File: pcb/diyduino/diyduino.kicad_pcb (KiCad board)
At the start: 2 copper layers, 22 parts, among them U1 ATMEGA328-PU, U2 L7805, Y1 16MHz

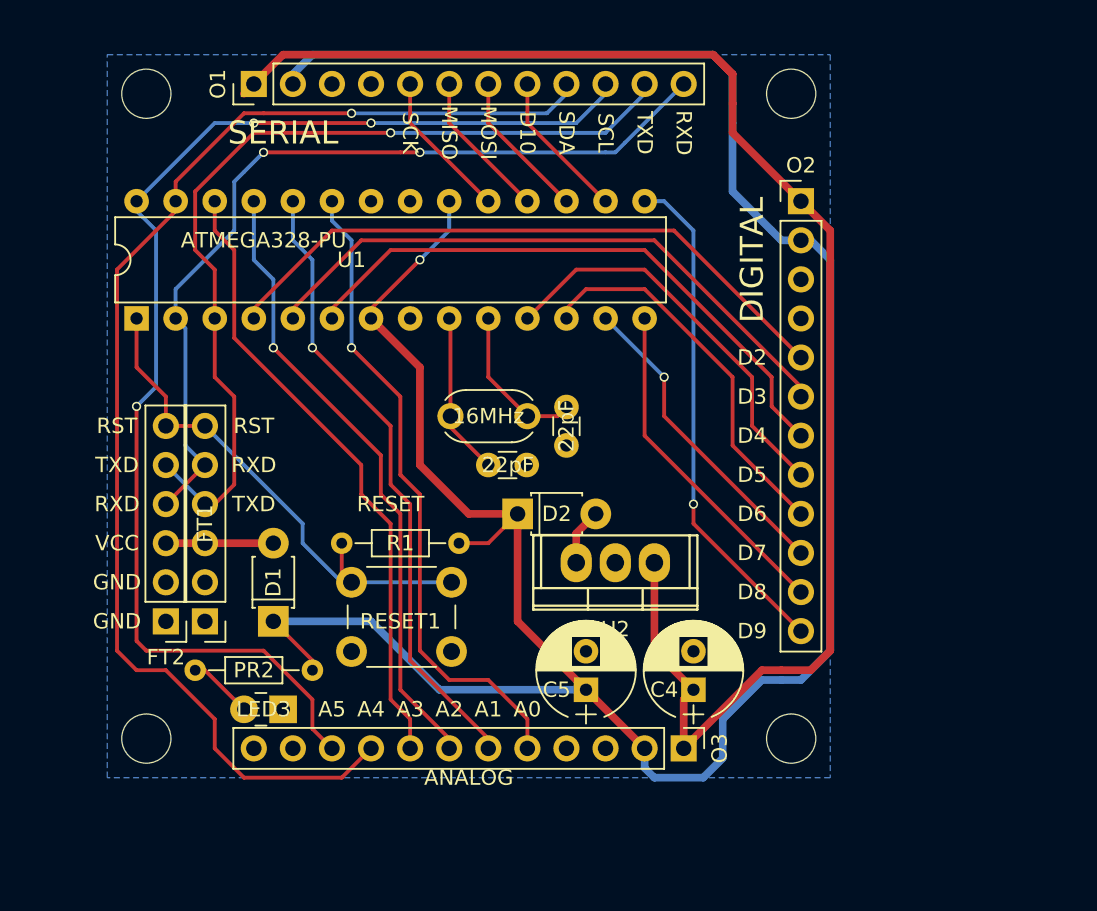
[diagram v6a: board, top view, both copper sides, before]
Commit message: Added a Rotary Encoder module. Tidied up a couple of modules before printing them.
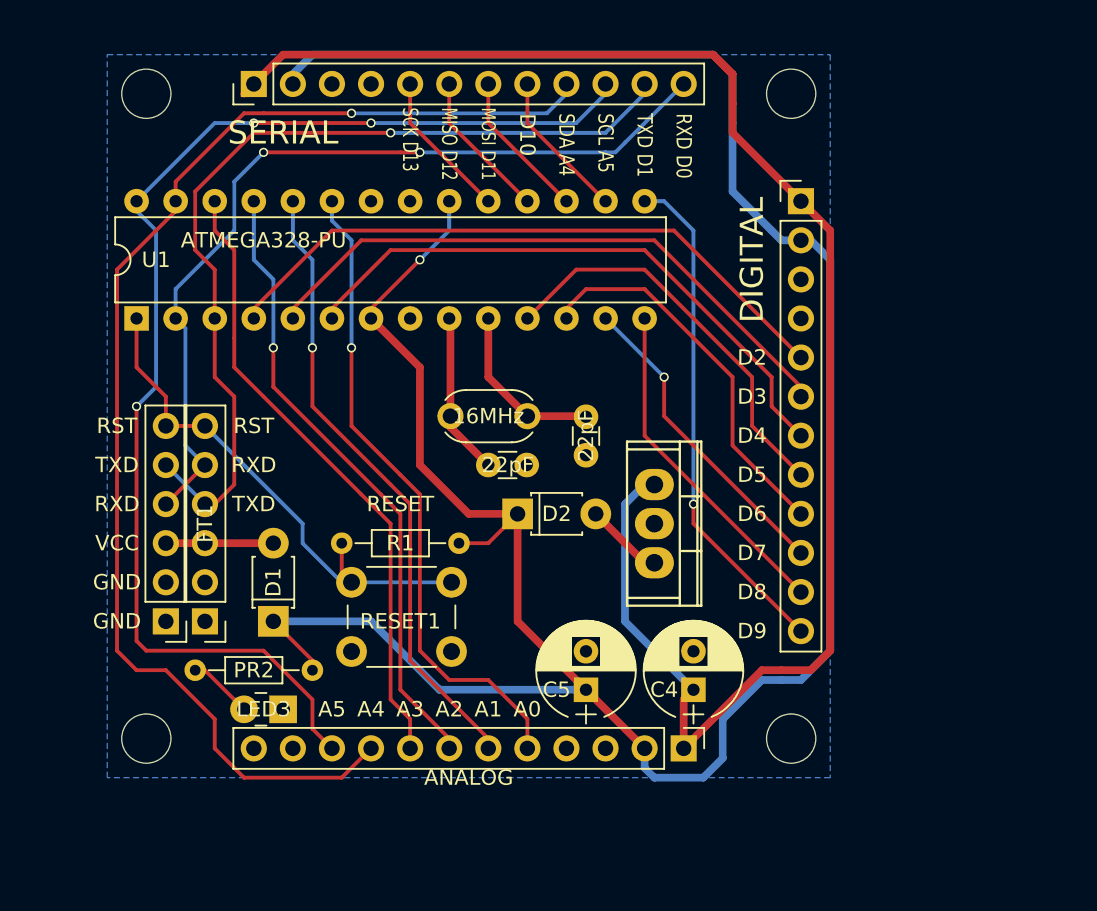
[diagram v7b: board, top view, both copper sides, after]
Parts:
- moved U2 3.59 mm to (145.4, 62.9), turned to 270 degrees
- moved C3 1.42 mm to (141.0, 58.4)
- gave numbers to parts that had none: 1
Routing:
- net /VIN: track 102.0 -> 109.1 mm
- net Net-(D2-Pad2): track 3.70 -> 5.13 mm
- net Net-(C3-Pad2): track 10.2 -> 11.3 mm
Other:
- board text added: "Diyduino v1.1 http://nickthecoder.co.uk"
- board text added: "MISO D12"
- board text added: "MOSI D11"
- board text added: "RXD D0"
- board text added: "SCK D13"
- board text added: "SCL A5"
- board text added: "SDA A4"
- board text added: "TXD D1"
- board text removed: "Diyduino V1.0 http://nickthecoder.co.uk"
- board text removed: "MISO"
- board text removed: "MOSI"
- board text removed: "SCK"
- board text removed: "SCL"
- board text removed: "SDA"

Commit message: Added README.md for each of the modules, plus a few minor tweaks to PCB layouts while writing the text.
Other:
- board text added: "S"
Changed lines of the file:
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@@
     (area 108.585 30.775 158.115001 80.645001)
     (thickness 1.6)
-    (drawings 36)
+    (drawings 38)
     (tracks 255)
     (zones 0)
@@
   )
   (setup
-    (last_trace_width 0.5)
+    (last_trace_width 0.25)
     (user_trace_width 0.5)
     (user_trace_width 0.5)
@@
     )
   )
+  (gr_text S (at 124.46 73.025) (layer F.SilkS)
+    (effects (font (size 1 1) (thickness 0.2)))
+  )
+  (gr_text S (at 127 73.025) (layer F.SilkS)
+    (effects (font (size 1 1) (thickness 0.2)))
+  )
   (gr_text ANALOG (at 133.35 79.375) (layer F.SilkS)
